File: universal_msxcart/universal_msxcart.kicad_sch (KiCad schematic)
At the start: 9 parts, among them J1 Conn_01x21_Pin, P1 CONN_02X25, U1 74HC244, U2 74HC244, U3 74HC244, U4 TXB0108PW, U5 74LS08, U6 74LS05, U7 74LS139

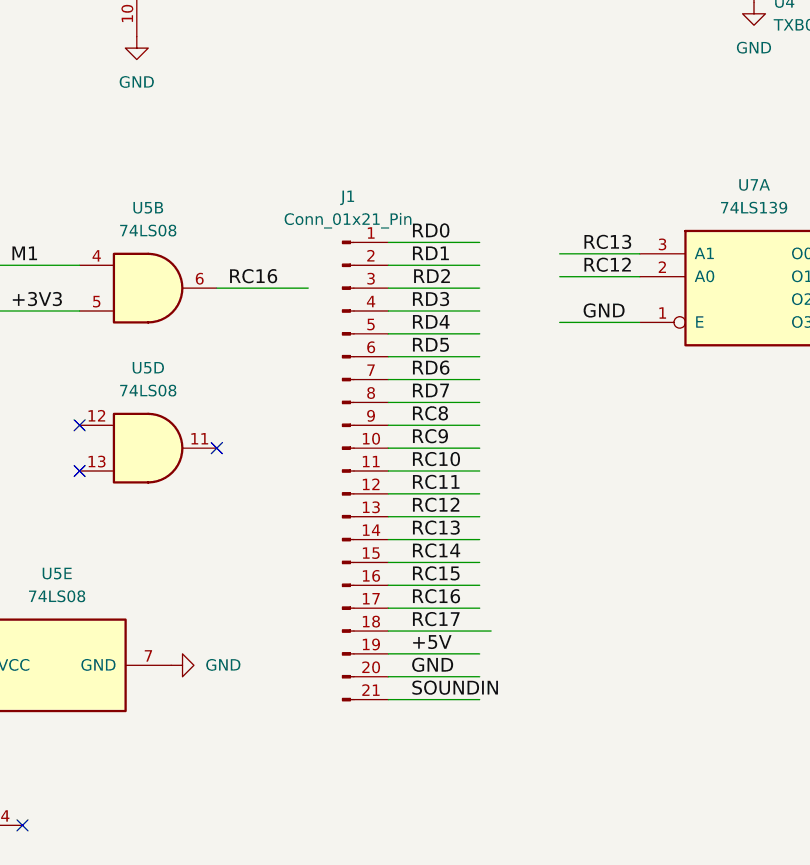
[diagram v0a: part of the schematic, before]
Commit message: epm240_msxcart/epm240_msxcart.kicad_pcb epm240_msxcart/epm240_msxcart.kicad_prl epm240_msxcart/epm240_msxcart.kicad_sch epm240_msxcart/fp-info-cache epm240_msxcart/freerouting.dsn epm240_msxcart/freerouting.ses universal_msxcart/.gitignore universal_msxcart/fp-info-cache universal_msxcart/universal_msxcart.kicad_pcb universal_msxcart/universal_msxcart.kicad_prl universal_msxcart/universal_msxcart.kicad_sch
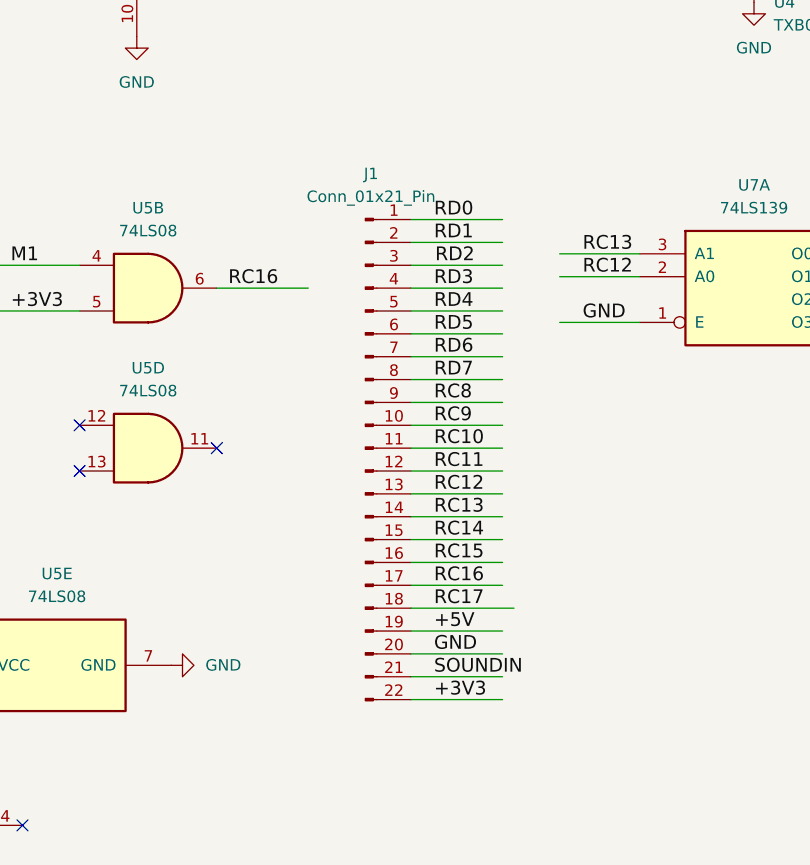
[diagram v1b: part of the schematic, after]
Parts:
- removed J1: Conn_01x21_Pin, Connector_PinSocket_2.54mm:PinSocket_1x21_P2.54mm_Horizontal, symbol Connector:Conn_01x21_Pin
- added J1: Conn_01x21_Pin, Connector_PinSocket_2.54mm:PinSocket_1x22_P2.54mm_Horizontal, symbol Connector:Conn_01x22_Pin
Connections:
- net +3V3: now also J1.22 (Pin_22)
- net +5V: now also J1.19 (Pin_19)
- net GND: now also J1.20 (Pin_20)
- net RC10: now also J1.11 (Pin_11)
- net RC11: now also J1.12 (Pin_12)
- net RC12: now also J1.13 (Pin_13)
- net RC13: now also J1.14 (Pin_14)
- net RC14: now also J1.15 (Pin_15)
- net RC15: now also J1.16 (Pin_16)
- net RC16: now also J1.17 (Pin_17)
- net RC17: now also J1.18 (Pin_18)
- net RC8: now also J1.9 (Pin_9)
- net RC9: now also J1.10 (Pin_10)
- net RD0: now also J1.1 (Pin_1)
- net RD1: now also J1.2 (Pin_2)
- net RD2: now also J1.3 (Pin_3)
- net RD3: now also J1.4 (Pin_4)
- net RD4: now also J1.5 (Pin_5)
- net RD5: now also J1.6 (Pin_6)
- net RD6: now also J1.7 (Pin_7)
- net RD7: now also J1.8 (Pin_8)
- net SOUNDIN: now also J1.21 (Pin_21)

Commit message: universal_msxcart/universal_msxcart.kicad_pcb universal_msxcart/universal_msxcart.kicad_pro universal_msxcart/universal_msxcart.kicad_sch
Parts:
- added unit 3 of U7
- added unit 2 of U7
- U1, U2, U3: value 74HC244 -> 74HC245; symbol 74xx:74HC244 -> 74xx:74HC245
- U6: value 74LS05 -> 74LS07
- U6: value 74LS05 -> 74LS07; symbol 74xx:74LS05 -> 74xx:74LS07
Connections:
- net 5V0 is gone; now on net +5V: P1.45 (Pin_45), P1.47 (Pin_47)
- net +3V3: now also U1.1 (A->B), U2.1 (A->B), U3.1 (A->B), U7.16 (VCC)
- net A0: now also U2.3 (A1); no longer U2.4 (1A1)
- net A10: now also U1.7 (A5); no longer U1.15 (2A1)
- net A11: now also U1.6 (A4); no longer U1.17 (2A0)
- net A12: now also U1.5 (A3); no longer U1.8 (1A3)
- net A13: now also U1.4 (A2); no longer U1.6 (1A2)
- net A14: now also U1.3 (A1); no longer U1.4 (1A1)
- net A2: now also U2.5 (A3); no longer U2.8 (1A3)
- net A3: now also U2.4 (A2); no longer U2.6 (1A2)
- net A4: now also U2.7 (A5); no longer U2.15 (2A1)
- net A5: now also U2.6 (A4); no longer U2.17 (2A0)
- net A6: now also U2.9 (A7); no longer U2.11 (2A3)
- net A7: now also U2.8 (A6); no longer U2.13 (2A2)
- net A8: now also U1.9 (A7); no longer U1.11 (2A3)
- net A9: now also U1.8 (A6); no longer U1.13 (2A2)
- net ADDRH: no longer U1.1 (1OE)
- net ADDRL: no longer U2.1 (1OE)
- net CLK: now also U3.9 (A7); no longer U3.11 (2A3)
- net GND: now also U7.8 (GND); no longer U3.1 (1OE)
- net IORQ: now also U3.5 (A3); no longer U3.8 (1A3)
- net M1: now also U3.8 (A6); no longer U3.13 (2A2)
- net MREQ: now also U3.4 (A2); no longer U3.6 (1A2)
- net RC10: now also U3.17 (B1); no longer U3.16 (1Y1)
- net RC16: no longer U3.5 (2Y1)
- net RC17: no longer U3.3 (2Y0)
- net RC9: now also U3.15 (B3); no longer U3.12 (1Y3)
- net RD: now also U3.3 (A1); no longer U3.4 (1A1)
- net RD0: now also U1.11 (B7), U2.17 (B1); no longer U1.9 (2Y3), U2.16 (1Y1)
- net RD1: now also U1.12 (B6); no longer U1.7 (2Y2)
- net RD2: now also U1.13 (B5), U2.15 (B3); no longer U1.5 (2Y1), U2.12 (1Y3)
- net RD3: now also U1.14 (B4), U2.16 (B2); no longer U1.3 (2Y0), U2.14 (1Y2)
- net RD4: now also U1.15 (B3), U2.13 (B5); no longer U1.12 (1Y3), U2.5 (2Y1)
- net RD5: now also U1.16 (B2), U2.14 (B4); no longer U1.14 (1Y2), U2.3 (2Y0)
- net RD6: now also U1.17 (B1), U2.11 (B7); no longer U1.16 (1Y1), U2.9 (2Y3)
- net RD7: now also U2.12 (B6); no longer U2.7 (2Y2)
- net RESET: now also U3.6 (A4); no longer U3.17 (2A0)
- net WR: now also U3.7 (A5); no longer U3.15 (2A1)
- no-connect marks 22 -> 29
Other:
- note added: "RC8 MREQ/IORQ (REQ) RC9 IORQ RC10 RD RC11 SLTSL RC12 ADDRL/ADDRH RC13 DATA RC14 WAIT RC15 INT RC16 M1 RC17 RESET RC16"
- moved on the sheet: U1, U2, U3, U4

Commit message: universal_msxcart.kicad_pro universal_msxcart.kicad_sch
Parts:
- removed U5: 74LS08, Package_SO:SOIC-14_3.9x8.7mm_P1.27mm, symbol 74xx:74LS08
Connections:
- net RC16: now also U3.12 (B6)
- net RC17: now also U3.14 (B4)
- net RC8: now also U3.16 (B2)
- no-connect marks 29 -> 26
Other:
- note added: "RC8 MREQ RC9 IORQ RC10 RD RC11 SLTSL RC12 ADDRL/ADDRH RC13 ADDR/DATA RC14 WAIT RC15 INT RC16 M1 RC17 RESET"
- note removed: "RC8 MREQ/IORQ (REQ) RC9 IORQ RC10 RD RC11 SLTSL RC12 ADDRL/ADDRH RC13 DATA RC14 WAIT RC15 INT RC16 M1 RC17 RESET RC16"
- moved on the sheet: U6A, U6B, U6C, U6D, U6E, U6F, U6G
